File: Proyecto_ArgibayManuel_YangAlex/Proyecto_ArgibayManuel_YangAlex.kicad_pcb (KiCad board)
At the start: 2 copper layers, 133 x 66 mm, 67 parts, among them IC1 LM1117, J1 Conn_01x02, J10 Con_1x2, J11 Con_1x2, J12 Con_ICSP, J2 Conn_01x01, J3 Con_1x2, J4 Con_1x2, J5 Con_1x2, J6 Con_1x2, J7 Conn_01x03, J8 Conn_01x03, J9 Conn_01x03_Pin, K1 RT314012, K2 RT314012, Q1 2N2222, Q2 2N2222, SW1 SW_Push, SW2 SW_Push, SW3 SW_Push, SW4 SW_Push, U1 PIC18F258-I_SO, U2 HDC2010YPAR, U3 LT1716IS5TRMPBF, U4 LT1716IS5TRMPBF, U5 TXS0108EPW, U6 DRV8871DDA, U7 DRV8871DDA, U8 MCP2551-I-P, X1 DB9, X2 DB9, Y1 Crystal

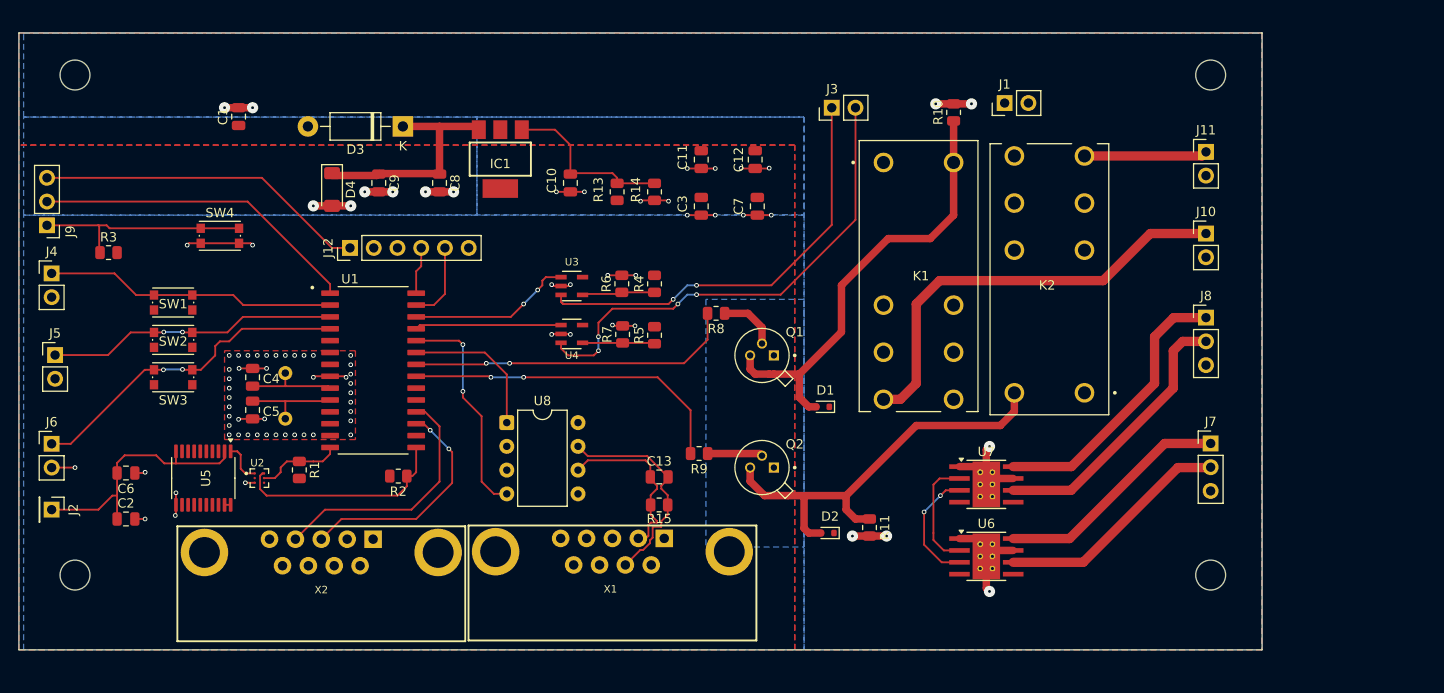
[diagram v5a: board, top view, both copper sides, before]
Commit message: Cambio del sensor
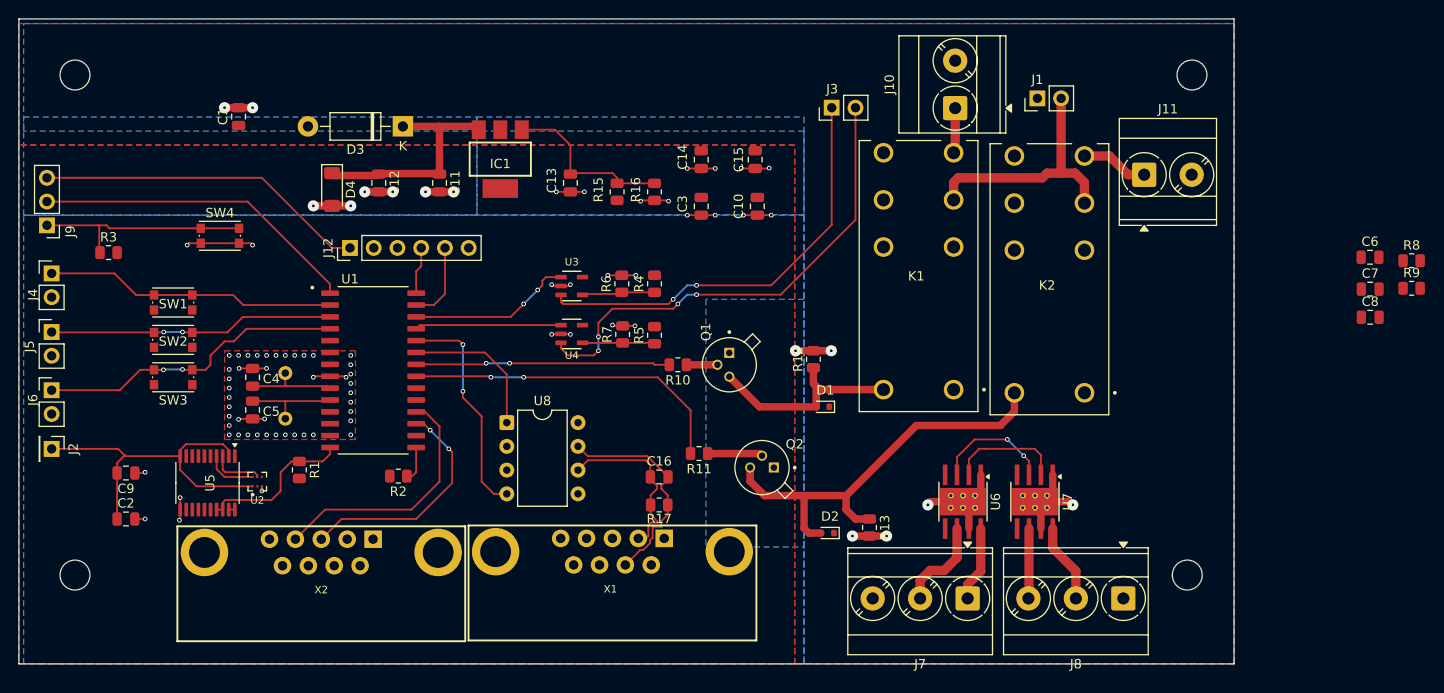
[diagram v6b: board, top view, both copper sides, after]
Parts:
- added C6: 100nF, Capacitor_SMD:C_0805_2012Metric, F.Cu at (240.6, 56.5)
- added C7: 100nF, Capacitor_SMD:C_0805_2012Metric, F.Cu at (240.6, 59.9)
- added C8: 100nF, Capacitor_SMD:C_0805_2012Metric, F.Cu at (240.6, 62.9)
- added R8: 4.7K, Resistor_SMD:R_0805_2012Metric, F.Cu at (245.0, 56.9)
- added R9: 4.7K, Resistor_SMD:R_0805_2012Metric, F.Cu at (245.0, 59.8)
- J10, J11: footprint Connector_PinHeader_2.54mm:PinHeader_1x02_P2.54mm_Vertical -> TerminalBlock_Phoenix:TerminalBlock_Phoenix_MKDS-3-2-5.08_1x02_P5.08mm_Horizontal
- J7, J8: footprint Connector_PinHeader_2.54mm:PinHeader_1x03_P2.54mm_Vertical -> TerminalBlock_Phoenix:TerminalBlock_Phoenix_MKDS-3-3-5.08_1x03_P5.08mm_Horizontal
- moved J8 31.3 mm to (214.2, 93.0), turned to 180 degrees
- moved J7 30.8 mm to (197.5, 93.0), turned to 180 degrees
- moved R12 30.4 mm to (181.0, 67.4)
- moved J10 30.0 mm to (196.2, 40.5), turned to 90 degrees
- moved J11 7.05 mm to (216.4, 47.7)
- moved R10 6.85 mm to (166.5, 68.0)
- moved J2 6.50 mm to (99.5, 77.0)
- moved U6 6.36 mm to (197.0, 82.7), turned to -90 degrees
- moved J6 5.73 mm to (99.5, 70.7)
- moved U7 5.52 mm to (204.7, 82.7), turned to -90 degrees
- moved Q1 3.64 mm to (172.0, 68.0), turned to -90 degrees
- moved J1 3.54 mm to (205.0, 39.5)
- moved REF** 2.50 mm to (221.0, 90.5)
- moved J5 2.49 mm to (99.5, 64.5)
- moved REF** 2.00 mm to (221.5, 37.0)
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- renumbered C7 to C10, C8 to C11, C9 to C12, C10 to C13, C11 to C14, C12 to C15, C13 to C16, C6 to C9, R8 to R10, R9 to R11, R10 to R12, R11 to R13, R13 to R15, R14 to R16, R15 to R17
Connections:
- J8 pad 1: Motor_derecho_1 -> GNDPWR
- J8 pad 2: Motor_derecho_2 -> Motor_derecho_1
- J8 pad 3: GNDPWR -> Motor_derecho_2
- R1 pad 1: SCL -> SCL_5V
- R2 pad 1: SDA -> SDA_5V
- U1 pad 14: SCL -> SCL_5V
- U1 pad 15: SDA -> SDA_5V
- U2 pad A1: Net-(U2-VDD) -> +3.3V
- U2 pad A2: SDA -> SDA_3,3V
- U2 pad B2: SCL -> SCL_3,3V
- U5 pad 1: Net-(U2-VDD) -> unconnected-(U5-A1-Pad1)
- U5 pad 17: unconnected-(U5-B3-Pad17) -> SCL_5V
- U5 pad 18: unconnected-(U5-B2-Pad18) -> SCL_5V
- U5 pad 3: unconnected-(U5-A2-Pad3) -> SCL_3,3V
- U5 pad 4: unconnected-(U5-A3-Pad4) -> SDA_3,3V
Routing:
- net Bomba: track 46.8 -> 4.84 mm
- net VBat: track 0.00 -> 26.9 mm
- net Net-(D1-A): track 48.2 -> 22.3 mm
- net SDA: track 23.3 -> 0.00 mm
- net Motor_derecho_2: track 29.6 -> 7.59 mm
- net Motor_derecho_1: track 30.2 -> 8.50 mm
- net Motor_Izquierdo_1: track 25.3 -> 8.06 mm
- net SCL_5V: track 0.00 -> 16.9 mm
- net Motor_izquierdo_2: track 25.3 -> 9.99 mm
- net +3.3V: track 28.1 -> 38.2 mm
- net SCL: track 9.12 -> 0.00 mm
- net C_R_Bombas_agua: track 35.1 -> 27.2 mm
- net Calefactor: track 13.3 -> 7.22 mm
- net SCL_3,3V: track 0.00 -> 5.58 mm
- net SDA_3,3V: track 0.00 -> 5.58 mm
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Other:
- board size 133 x 66 mm -> 130 x 69 mm

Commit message: Arreglo layout y esquematico (DRC correcto)
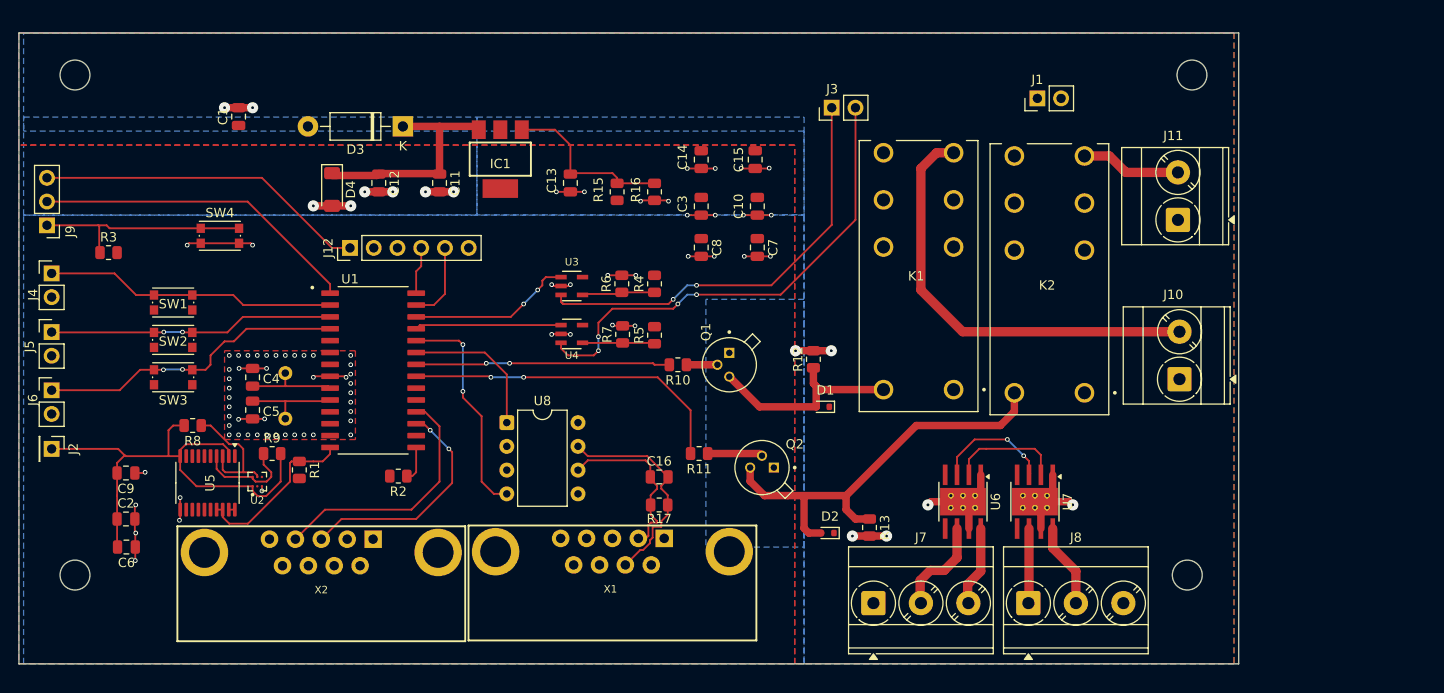
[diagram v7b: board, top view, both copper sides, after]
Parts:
- moved C6 136.6 mm to (107.5, 87.5), turned to 180 degrees
- moved R8 131.6 mm to (114.6, 74.5), turned to 180 degrees
- moved R9 123.2 mm to (123.1, 77.5)
- moved C8 72.0 mm to (169.0, 55.5), turned to -90 degrees
- moved C7 65.7 mm to (175.0, 55.5), turned to -90 degrees
- moved J10 37.6 mm to (220.2, 69.5)
- moved J8 10.2 mm to (204.0, 93.5), turned to 0 degrees
- moved J7 10.1 mm to (187.4, 93.5), turned to 0 degrees
- moved J11 6.03 mm to (220.0, 52.5), turned to 90 degrees
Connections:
- J10 pad 1: Bomba -> GNDPWR
- J10 pad 2: GNDPWR -> Bomba
- J11 pad 1: Calefactor -> GNDPWR
- J11 pad 2: GNDPWR -> Calefactor
- J7 pad 1: Motor_Izquierdo_1 -> GNDPWR
- J7 pad 3: GNDPWR -> Motor_Izquierdo_1
- J8 pad 1: GNDPWR -> Motor_derecho_2
- J8 pad 3: Motor_derecho_2 -> GNDPWR
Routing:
- net Bomba: track 4.84 -> 46.9 mm
- net VBat: track 26.9 -> 0.00 mm
- net +3.3V: track 38.2 -> 53.2 mm
- net GND: track 49.6 -> 60.3 mm, vias 69 -> 75
- net SCL_3,3V: track 5.58 -> 13.1 mm
- net SDA_3,3V: track 5.58 -> 10.9 mm
- net Calefactor: track 7.22 -> 10.7 mm
- net SCL_5V: track 16.9 -> 18.2 mm
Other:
- board size 130 x 69 mm -> 130.5 x 67.5 mm
